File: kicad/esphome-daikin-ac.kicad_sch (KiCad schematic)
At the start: 7 parts, among them Q1 P2N2222, U1 XIAO ESP32C3, U2 DS18B20

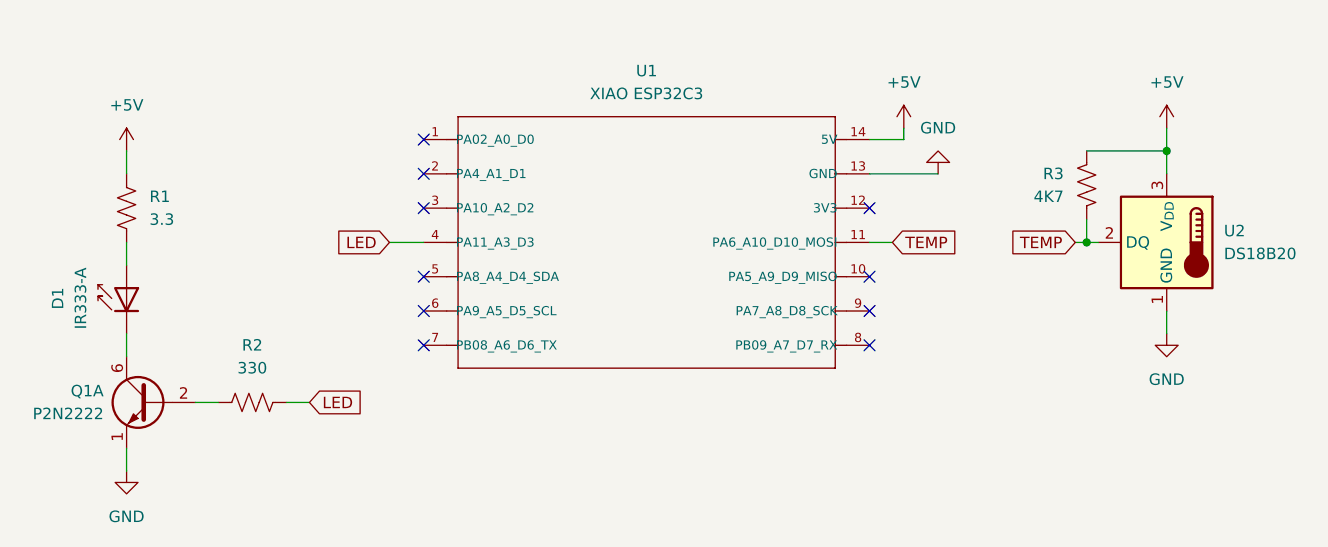
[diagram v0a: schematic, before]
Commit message: Fix errors in schematic
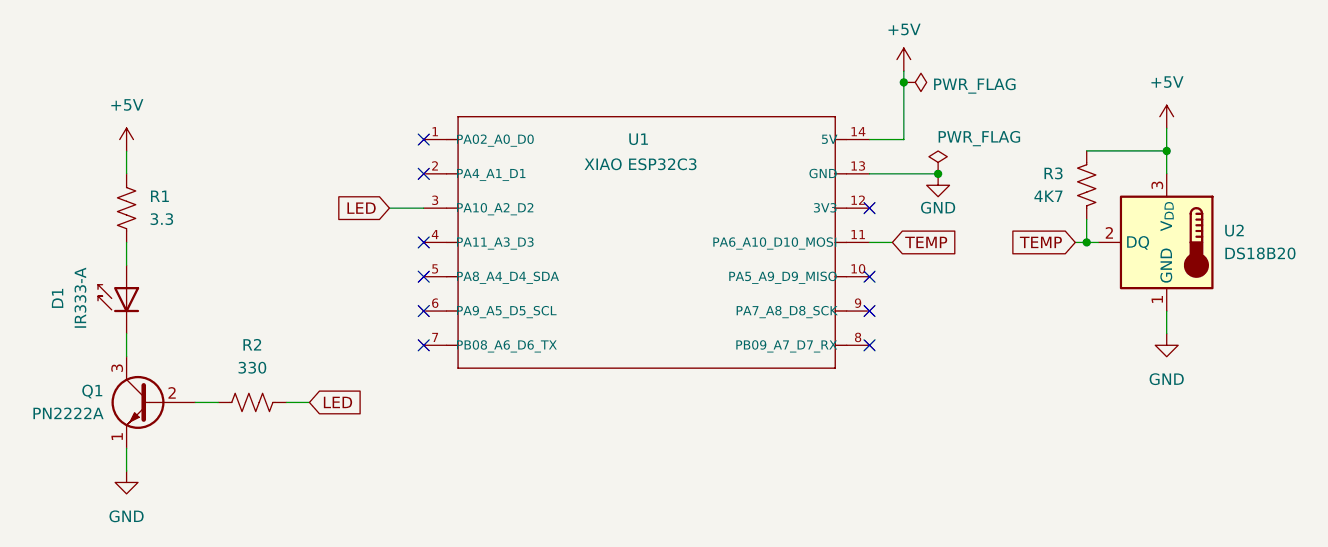
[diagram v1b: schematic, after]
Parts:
- removed Q1: P2N2222, Package_TO_SOT_SMD:SOT-363_SC-70-6, symbol Transistor_BJT:FFB2222A
- added Q1: PN2222A, Package_TO_SOT_THT:TO-92_Inline, symbol Transistor_BJT:PN2222A
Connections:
- net GND: now also Q1.1 (E)
- net LED: now also U1.3 (PA10_A2_D2); no longer U1.4 (PA11_A3_D3)
- net at R2.2: now also Q1.2 (B)
- net at D1.1 (K): now also Q1.3 (C)
